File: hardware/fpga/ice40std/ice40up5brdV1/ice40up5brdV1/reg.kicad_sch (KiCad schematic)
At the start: 16 parts, among them U1 ICE40UP5K-SG48ITR, U2 LTC3406ES5, U3 LTC3406ES5

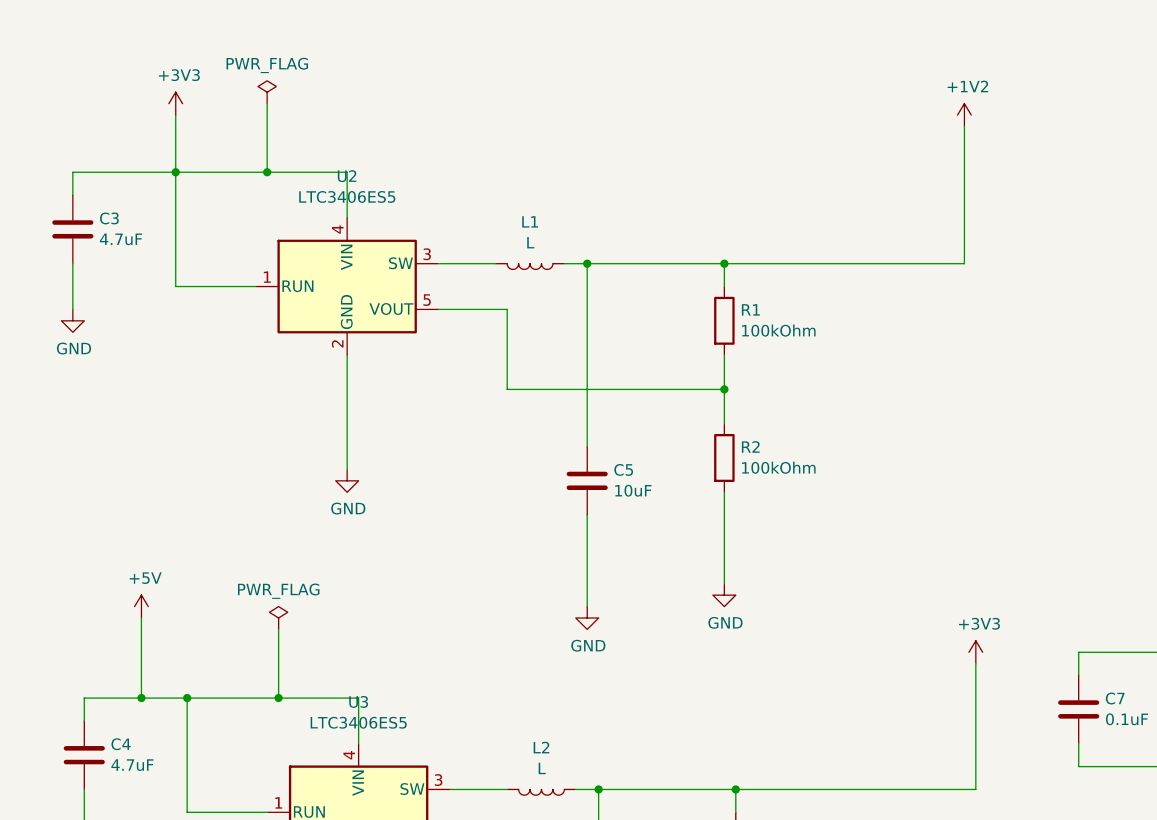
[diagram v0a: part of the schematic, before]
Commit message: started linear regs
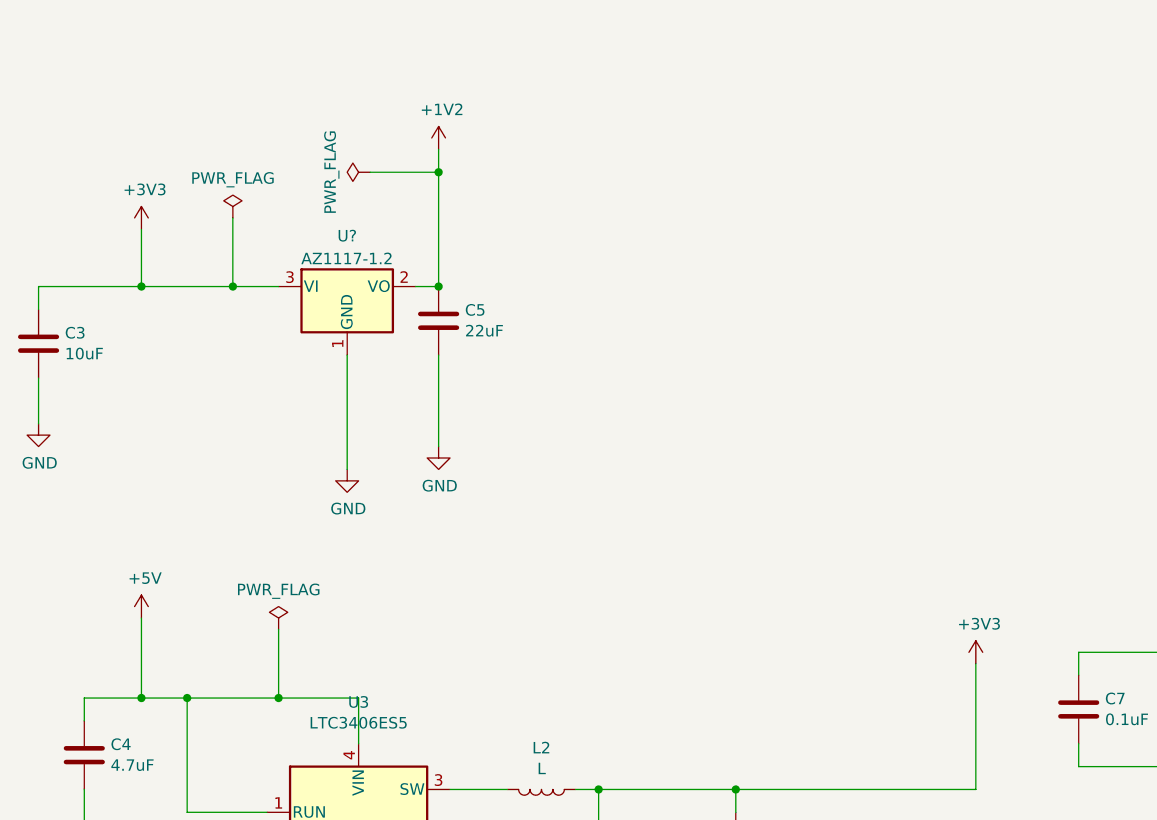
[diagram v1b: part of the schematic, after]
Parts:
- removed L1: L, Inductor_SMD:L_1210_3225Metric, symbol Device:L
- removed R1, R2: 100kOhm, Resistor_SMD:R_0402_1005Metric, symbol Device:R
- removed U2: LTC3406ES5, Package_TO_SOT_SMD:TSOT-23-5, symbol Regulator_Switching:LTC3406ES5
- added U?: AZ1117-1.2, symbol Regulator_Linear:AZ1117-1.2
- C3: value 4.7uF -> 10uF
- C5: value 10uF -> 22uF
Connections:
- net +1V2: now also U?.2 (VO)
- net +3V3: now also U?.3 (VI)
- net GND: now also U?.1 (GND)
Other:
- moved on the sheet: C3, C5

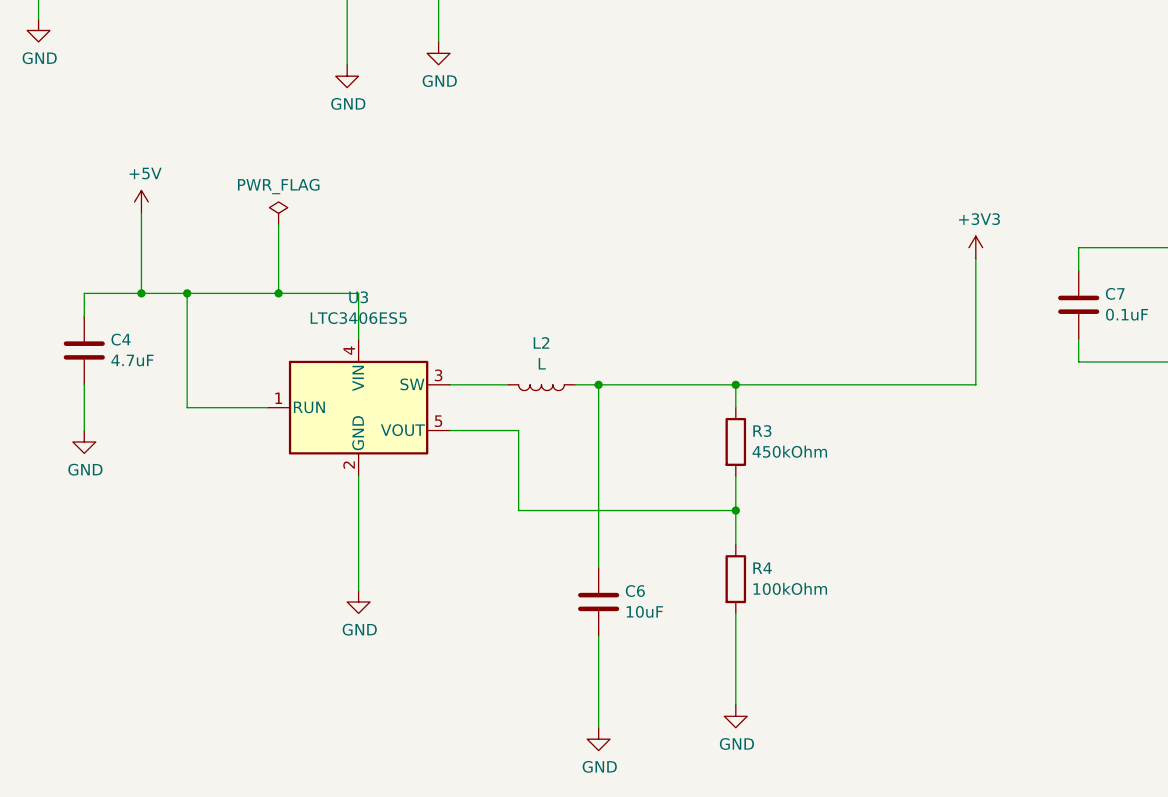
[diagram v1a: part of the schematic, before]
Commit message: started linear regs
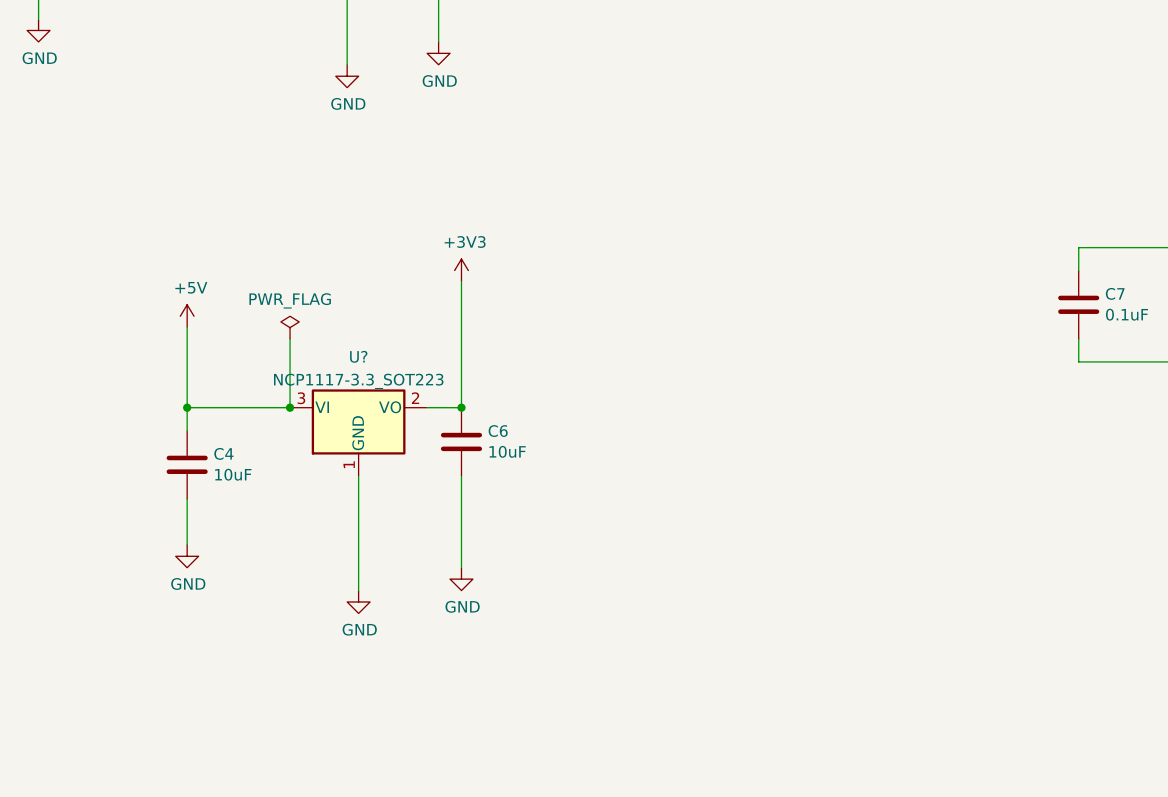
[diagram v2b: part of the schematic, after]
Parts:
- removed L2: L, Inductor_SMD:L_1210_3225Metric, symbol Device:L
- removed R3: 450kOhm, Resistor_SMD:R_0402_1005Metric, symbol Device:R
- removed R4: 100kOhm, Resistor_SMD:R_0402_1005Metric, symbol Device:R
- removed U3: LTC3406ES5, Package_TO_SOT_SMD:TSOT-23-5, symbol Regulator_Switching:LTC3406ES5
- added U?: NCP1117-3.3_SOT223, Package_TO_SOT_SMD:SOT-223-3_TabPin2, symbol Regulator_Linear:NCP1117-3.3_SOT223
- C4: value 4.7uF -> 10uF
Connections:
- net +3V3: now also U?.2 (VO)
- net +5V: now also U?.3 (VI)
- net GND: now also U?.1 (GND)
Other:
- moved on the sheet: C4, C6

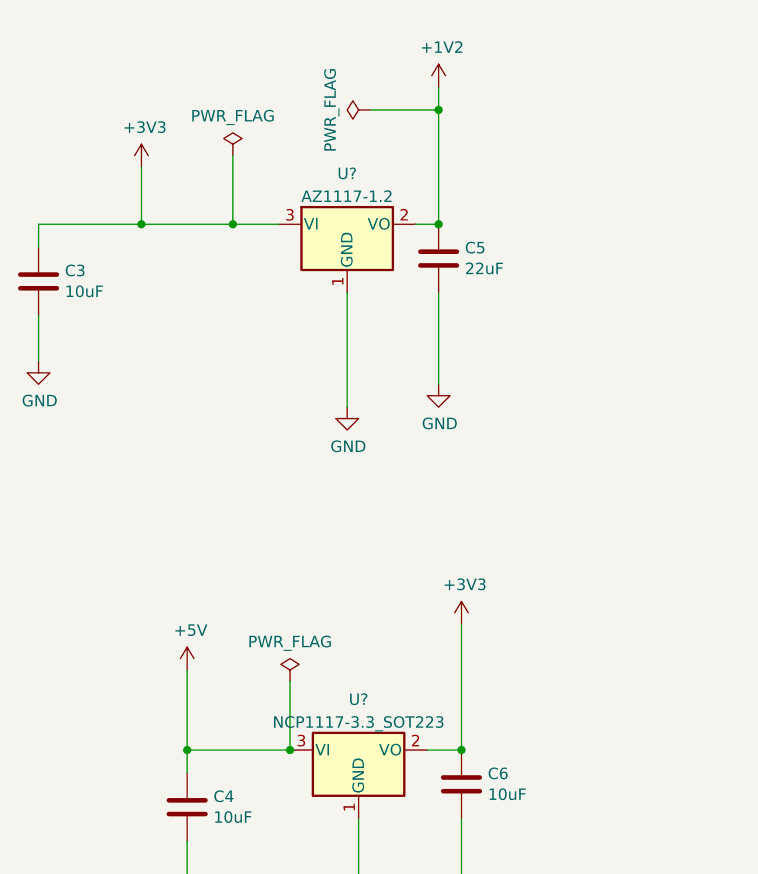
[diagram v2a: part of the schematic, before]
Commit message: started linear regs / Amphenol USB
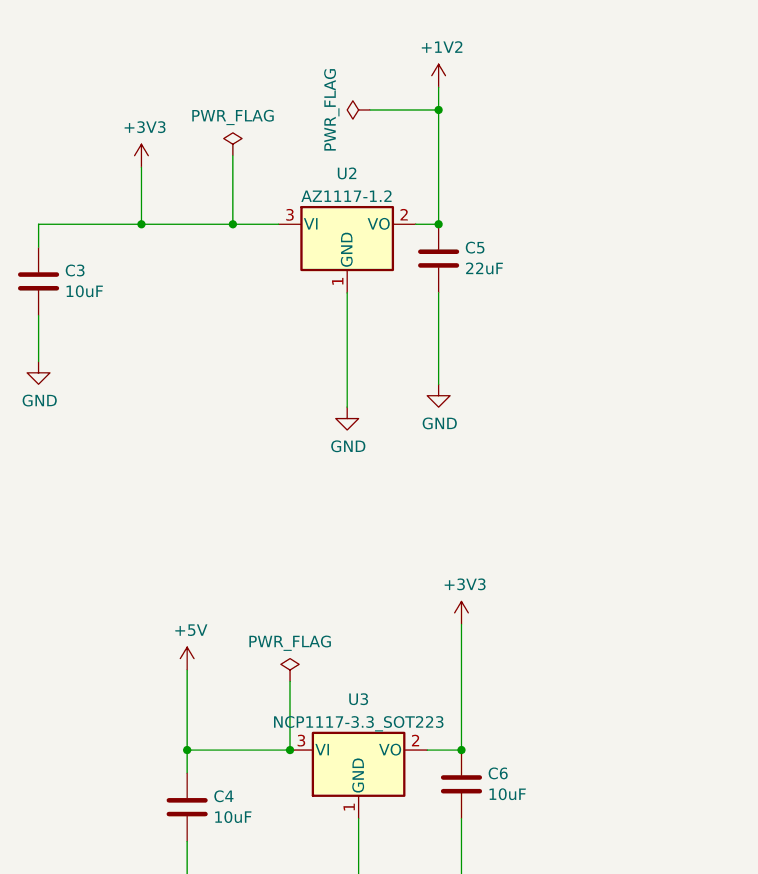
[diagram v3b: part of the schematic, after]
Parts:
- U2: renamed from U?; footprint (none) -> Package_TO_SOT_SMD:SOT-223-3_TabPin2
- gave numbers to parts that had none: 1
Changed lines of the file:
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@@
   (symbol (lib_id "power:PWR_FLAG") (at 60.96 66.04 90) (unit 1)
     (in_bom yes) (on_board yes)
-    (property "Reference" "#FLG?" (id 0) (at 59.055 66.04 0)
+    (property "Reference" "#FLG0101" (id 0) (at 59.055 66.04 0)
       (effects (font (size 1.27 1.27)) hide)
     )
@@
   (symbol (lib_id "Regulator_Linear:NCP1117-3.3_SOT223") (at 59.69 137.16 0) (unit 1)
     (in_bom yes) (on_board yes) (fields_autoplaced)
-    (property "Reference" "U?" (id 0) (at 59.69 131.5552 0))
+    (property "Reference" "U3" (id 0) (at 59.69 131.5552 0))
     (property "Value" "NCP1117-3.3_SOT223" (id 1) (at 59.69 134.0921 0))
     (property "Footprint" "Package_TO_SOT_SMD:SOT-223-3_TabPin2" (id 2) (at 59.69 132.08 0)
@@
   (symbol (lib_id "Regulator_Linear:AZ1117-1.2") (at 58.42 78.74 0) (unit 1)
     (in_bom yes) (on_board yes) (fields_autoplaced)
-    (property "Reference" "U?" (id 0) (at 58.42 73.1352 0))
+    (property "Reference" "U2" (id 0) (at 58.42 73.1352 0))
     (property "Value" "AZ1117-1.2" (id 1) (at 58.42 75.6721 0))
-    (property "Footprint" "" (id 2) (at 58.42 72.39 0)
+    (property "Footprint" "Package_TO_SOT_SMD:SOT-223-3_TabPin2" (id 2) (at 58.42 72.39 0)
       (effects (font (size 1.27 1.27) italic) hide)
     )

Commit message: pwm / lvds power / filters
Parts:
- added C16, C18: 10uF, Capacitor_SMD:C_0402_1005Metric, symbol Device:C
- added C17, C19: 10uF, Capacitor_SMD:C_0603_1608Metric, symbol Device:C
- added U6, U7: NCP1117-3.3_SOT223, Package_TO_SOT_SMD:SOT-223-3_TabPin2, symbol Regulator_Linear:NCP1117-3.3_SOT223
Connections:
- net +5V: now also C16.1, C18.1, U6.3 (VI), U7.3 (VI)
- net GND: now also C16.2, C17.2, C18.2, C19.2, U6.1 (GND), U7.1 (GND)
- new net 3V3ANA: C19.1, U7.2 (VO)
- new net 3V3PWM: C17.1, U6.2 (VO)
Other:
- moved on the sheet: D1, U1D

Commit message: pwm / lvds power / filters
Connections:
- net +1V2: no longer U1.29 (VCCPLL)
- new net VCCPLL: U1.29 (VCCPLL)
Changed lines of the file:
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@@
   (junction (at 153.67 119.38) (diameter 0) (color 0 0 0 0)
   )
-  (junction (at 257.81 35.56) (diameter 0) (color 0 0 0 0)
-  )
   (junction (at 138.43 57.15) (diameter 0) (color 0 0 0 0)
   )
@@
   (junction (at 250.19 33.02) (diameter 0) (color 0 0 0 0)
   )
-  (wire (pts (xy 257.81 35.56) (xy 275.59 35.56))
-    (stroke (width 0) (type default) (color 0 0 0 0))
-  )
   (wire (pts (xy 255.27 60.96) (xy 255.27 68.58))
     (stroke (width 0) (type default) (color 0 0 0 0))
@@
     (stroke (width 0) (type default) (color 0 0 0 0))
   )
-  (wire (pts (xy 257.81 40.64) (xy 257.81 35.56))
-    (stroke (width 0) (type default) (color 0 0 0 0))
-  )
   (wire (pts (xy 52.07 129.54) (xy 52.07 137.16))
     (stroke (width 0) (type default) (color 0 0 0 0))
@@
     (stroke (width 0) (type default) (color 0 0 0 0))
   )
-  (wire (pts (xy 255.27 35.56) (xy 257.81 35.56))
+  (wire (pts (xy 255.27 35.56) (xy 275.59 35.56))
     (stroke (width 0) (type default) (color 0 0 0 0))
   )
@@
       (effects (font (size 1.27 1.27)) (justify left) hide)
     )
+  )
+  (global_label "VCCPLL" (shape input) (at 257.81 40.64 90) (fields_autoplaced)
+    (effects (font (size 1.27 1.27)) (justify left))
+    (property "Intersheet References" "${INTERSHEET_REFS}" (id 0) (at 257.7306 31.361 90)
+      (effects (font (size 1.27 1.27)) (justify left) hide)
+    )

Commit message: pwm / lvds power / filters
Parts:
- added C?: 10uF, symbol Device:C
- added C?: o.1uF, symbol Device:C
- added R?: 100, symbol Device:R
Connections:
- net +1V2: now also R?.2
- net GND: now also C?.2, C?.2
- net VCCPLL: now also C?.1, C?.1, R?.1
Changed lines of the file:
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@@
   (junction (at 52.07 137.16) (diameter 0) (color 0 0 0 0)
   )
+  (junction (at 179.07 71.12) (diameter 0) (color 0 0 0 0)
+  )
   (junction (at 119.38 57.15) (diameter 0) (color 0 0 0 0)
   )
@@
   (junction (at 45.72 78.74) (diameter 0) (color 0 0 0 0)
   )
+  (junction (at 189.23 71.12) (diameter 0) (color 0 0 0 0)
+  )
   (junction (at 153.67 119.38) (diameter 0) (color 0 0 0 0)
   )
@@
     (stroke (width 0) (type default) (color 0 0 0 0))
   )
+  (wire (pts (xy 189.23 71.12) (xy 189.23 77.47))
+    (stroke (width 0) (type default) (color 0 0 0 0))
+  )
   (wire (pts (xy 119.38 49.53) (xy 119.38 57.15))
     (stroke (width 0) (type default) (color 0 0 0 0))
@@
     (stroke (width 0) (type default) (color 0 0 0 0))
   )
+  (wire (pts (xy 179.07 71.12) (xy 189.23 71.12))
+    (stroke (width 0) (type default) (color 0 0 0 0))
+  )
   (wire (pts (xy 205.74 113.03) (xy 205.74 121.92))
     (stroke (width 0) (type default) (color 0 0 0 0))
   )
+  (wire (pts (xy 189.23 85.09) (xy 189.23 92.71))
+    (stroke (width 0) (type default) (color 0 0 0 0))
+  )
   (wire (pts (xy 245.11 33.02) (xy 250.19 33.02))
     (stroke (width 0) (type default) (color 0 0 0 0))
@@
     (stroke (width 0) (type default) (color 0 0 0 0))
   )
+  (wire (pts (xy 179.07 71.12) (xy 179.07 77.47))
+    (stroke (width 0) (type default) (color 0 0 0 0))
+  )
   (wire (pts (xy 58.42 86.36) (xy 58.42 99.06))
     (stroke (width 0) (type default) (color 0 0 0 0))
@@
     (stroke (width 0) (type default) (color 0 0 0 0))
   )
+  (wire (pts (xy 175.26 71.12) (xy 179.07 71.12))
+    (stroke (width 0) (type default) (color 0 0 0 0))
+  )
   (wire (pts (xy 107.95 48.26) (xy 107.95 57.15))
     (stroke (width 0) (type default) (color 0 0 0 0))
@@
     (stroke (width 0) (type default) (color 0 0 0 0))
   )
+  (wire (pts (xy 189.23 71.12) (xy 194.31 71.12))
+    (stroke (width 0) (type default) (color 0 0 0 0))
+  )
   (wire (pts (xy 275.59 35.56) (xy 275.59 29.21))
     (stroke (width 0) (type default) (color 0 0 0 0))
@@
     (stroke (width 0) (type default) (color 0 0 0 0))
   )
+  (wire (pts (xy 201.93 71.12) (xy 208.28 71.12))
+    (stroke (width 0) (type default) (color 0 0 0 0))
+  )
   (wire (pts (xy 35.56 72.39) (xy 35.56 78.74))
     (stroke (width 0) (type default) (color 0 0 0 0))
@@
   )
   (wire (pts (xy 59.69 144.78) (xy 59.69 157.48))
+    (stroke (width 0) (type default) (color 0 0 0 0))
+  )
+  (wire (pts (xy 179.07 85.09) (xy 179.07 92.71))
     (stroke (width 0) (type default) (color 0 0 0 0))
   )
@@
     (property "Intersheet References" "${INTERSHEET_REFS}" (id 0) (at 138.3506 33.1753 90)
       (effects (font (size 1.27 1.27)) (justify left) hide)
+    )
+  )
+  (global_label "VCCPLL" (shape input) (at 175.26 71.12 180) (fields_autoplaced)
+    (effects (font (size 1.27 1.27)) (justify right))
+    (property "Intersheet References" "${INTERSHEET_REFS}" (id 0) (at 165.981 71.0406 0)
+      (effects (font (size 1.27 1.27)) (justify right) hide)
     )
   )
@@
     (pin "1")
   )
+  (symbol (lib_id "power:+1V2") (at 208.28 71.12 0) (unit 1)
+    (in_bom yes) (on_board yes)
+    (property "Reference" "#PWR?" (id 0) (at 208.28 74.93 0)
+      (effects (font (size 1.27 1.27)) hide)
+    )
+    (property "Value" "+1V2" (id 1) (at 208.661 66.7258 0))
+    (property "Footprint" "" (id 2) (at 208.28 71.12 0)
+      (effects (font (size 1.27 1.27)) hide)
+    )
+    (property "Datasheet" "" (id 3) (at 208.28 71.12 0)
+      (effects (font (size 1.27 1.27)) hide)
+    )
+    (pin "1")
+  )
   (symbol (lib_id "power:+5V") (at 107.95 48.26 0) (unit 1)
     (in_bom yes) (on_board yes)
@@
     )
     (property "Datasheet" "" (id 3) (at 127 77.47 0)
+      (effects (font (size 1.27 1.27)) hide)
+    )
+    (pin "1")
+  )
+  (symbol (lib_id "power:GND") (at 179.07 92.71 0) (unit 1)
+    (in_bom yes) (on_board yes)
+    (property "Reference" "#PWR?" (id 0) (at 179.07 99.06 0)
+      (effects (font (size 1.27 1.27)) hide)
+    )
+    (property "Value" "GND" (id 1) (at 179.197 97.1042 0))
+    (property "Footprint" "" (id 2) (at 179.07 92.71 0)
+      (effects (font (size 1.27 1.27)) hide)
+    )
+    (property "Datasheet" "" (id 3) (at 179.07 92.71 0)
       (effects (font (size 1.27 1.27)) hide)
     )
@@
     (pin "3")
   )
+  (symbol (lib_id "Device:R") (at 198.12 71.12 90) (unit 1)
+    (in_bom yes) (on_board yes) (fields_autoplaced)
+    (property "Reference" "R?" (id 0) (at 198.12 66.4042 90))
+    (property "Value" "100" (id 1) (at 198.12 68.9411 90))
+    (property "Footprint" "" (id 2) (at 198.12 72.898 90)
+      (effects (font (size 1.27 1.27)) hide)
+    )
+    (property "Datasheet" "~" (id 3) (at 198.12 71.12 0)
+      (effects (font (size 1.27 1.27)) hide)
+    )
+    (pin "1")
+    (pin "2")
+  )
   (symbol (lib_id "Regulator_Linear:NCP1117-3.3_SOT223") (at 224.79 121.92 0) (unit 1)
     (in_bom yes) (on_board yes) (fields_autoplaced)
@@
     (pin "3")
   )
+  (symbol (lib_id "power:GND") (at 189.23 92.71 0) (unit 1)
+    (in_bom yes) (on_board yes)
+    (property "Reference" "#PWR?" (id 0) (at 189.23 99.06 0)
+      (effects (font (size 1.27 1.27)) hide)
+    )
+    (property "Value" "GND" (id 1) (at 189.357 97.1042 0))
+    (property "Footprint" "" (id 2) (at 189.23 92.71 0)
+      (effects (font (size 1.27 1.27)) hide)
+    )
+    (property "Datasheet" "" (id 3) (at 189.23 92.71 0)
+      (effects (font (size 1.27 1.27)) hide)
+    )
+    (pin "1")
+  )
+  (symbol (lib_id "Device:C") (at 179.07 81.28 0) (unit 1)
+    (in_bom yes) (on_board yes) (fields_autoplaced)
+    (property "Reference" "C?" (id 0) (at 181.991 80.4453 0)
+      (effects (font (size 1.27 1.27)) (justify left))
+    )
+    (property "Value" "10uF" (id 1) (at 181.991 82.9822 0)
+      (effects (font (size 1.27 1.27)) (justify left))
+    )
+    (property "Footprint" "" (id 2) (at 180.0352 85.09 0)
+      (effects (font (size 1.27 1.27)) hide)
+    )
+    (property "Datasheet" "~" (id 3) (at 179.07 81.28 0)
+      (effects (font (size 1.27 1.27)) hide)
+    )
+    (pin "1")
+    (pin "2")
+  )
   (symbol (lib_id "power:GND") (at 224.79 142.24 0) (unit 1)
     (in_bom yes) (on_board yes)
@@
       (effects (font (size 1.27 1.27)) hide)
     )
+    (pin "1")
+    (pin "2")
+  )
+  (symbol (lib_id "Device:C") (at 189.23 81.28 0) (unit 1)
+    (in_bom yes) (on_board yes) (fields_autoplaced)
+    (property "Reference" "C?" (id 0) (at 192.151 80.4453 0)
+      (effects (font (size 1.27 1.27)) (justify left))
+    )
+    (property "Value" "o.1uF" (id 1) (at 192.151 82.9822 0)
+      (effects (font (size 1.27 1.27)) (justify left))
+    )
+    (property "Footprint" "" (id 2) (at 190.1952 85.09 0)
+      (effects (font (size 1.27 1.27)) hide)
+    )
+    (property "Datasheet" "~" (id 3) (at 189.23 81.28 0)
+      (effects (font (size 1.27 1.27)) hide)
+    )
